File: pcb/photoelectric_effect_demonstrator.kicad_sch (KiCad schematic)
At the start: 0 parts

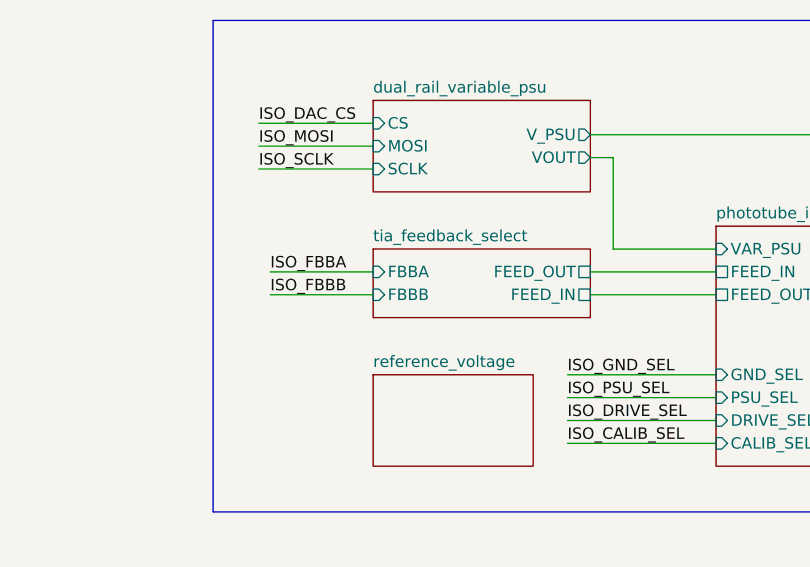
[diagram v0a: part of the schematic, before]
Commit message: reworked the digital isolation block
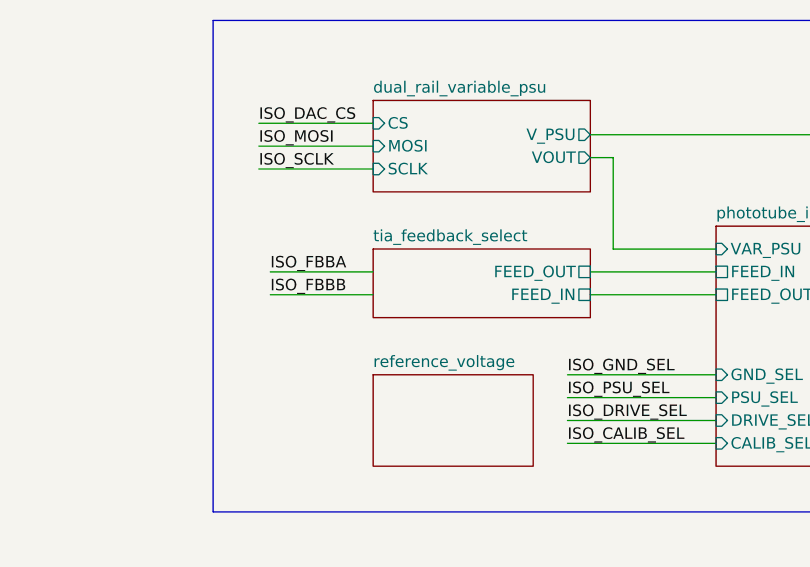
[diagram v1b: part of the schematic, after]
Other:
- sheet tia_feedback_select ports: added none; removed FBBA, FBBB
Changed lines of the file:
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@@
-			)
-		)
-		(pin "FBBA" input
-			(at 285.75 127 180)
-			(effects
-				(font
-					(size 1.27 1.27)
-				)
-				(justify left)
-			)
-		)
-		(pin "FBBB" input
-			(at 285.75 129.54 180)
-			(effects
-				(font
-					(size 1.27 1.27)
-				)
-				(justify left)
 			)
 		)
